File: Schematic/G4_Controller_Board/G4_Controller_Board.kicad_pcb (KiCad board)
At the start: 2 copper layers, 30 parts, among them J10 12 Volts In, J11 Preset A, J12 Voltmeter, J13 Preset B, J14 Preset C, J15 Combined Preset Connector, J16 Rev Trigger (Optional), J17 Fire Trigger, J18 Magazine Removal Trigger, J19 Rotary Encoder, J2 Screw_Terminal_01x02, J20 I2C Out, J21 ESC Right, J22 ESC Left, J25 IR LED Rec., J26 IR LED Emitter, J6 Solenoid, Q1 IRF540N, U1 Mini360, U2 ESP32-LOLIN32-Lite

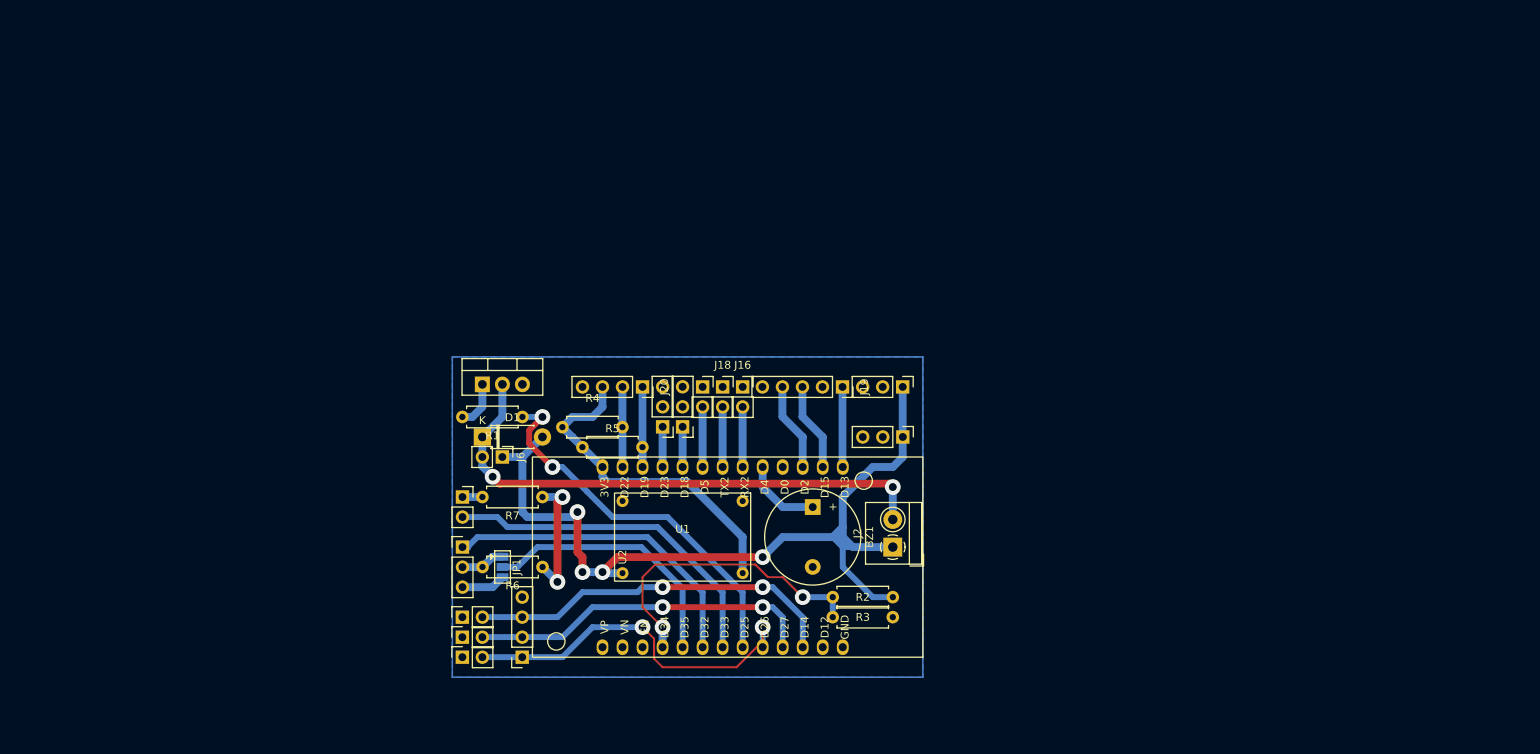
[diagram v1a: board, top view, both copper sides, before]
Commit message: begin work on new PCB
2 layers with fast decay driver
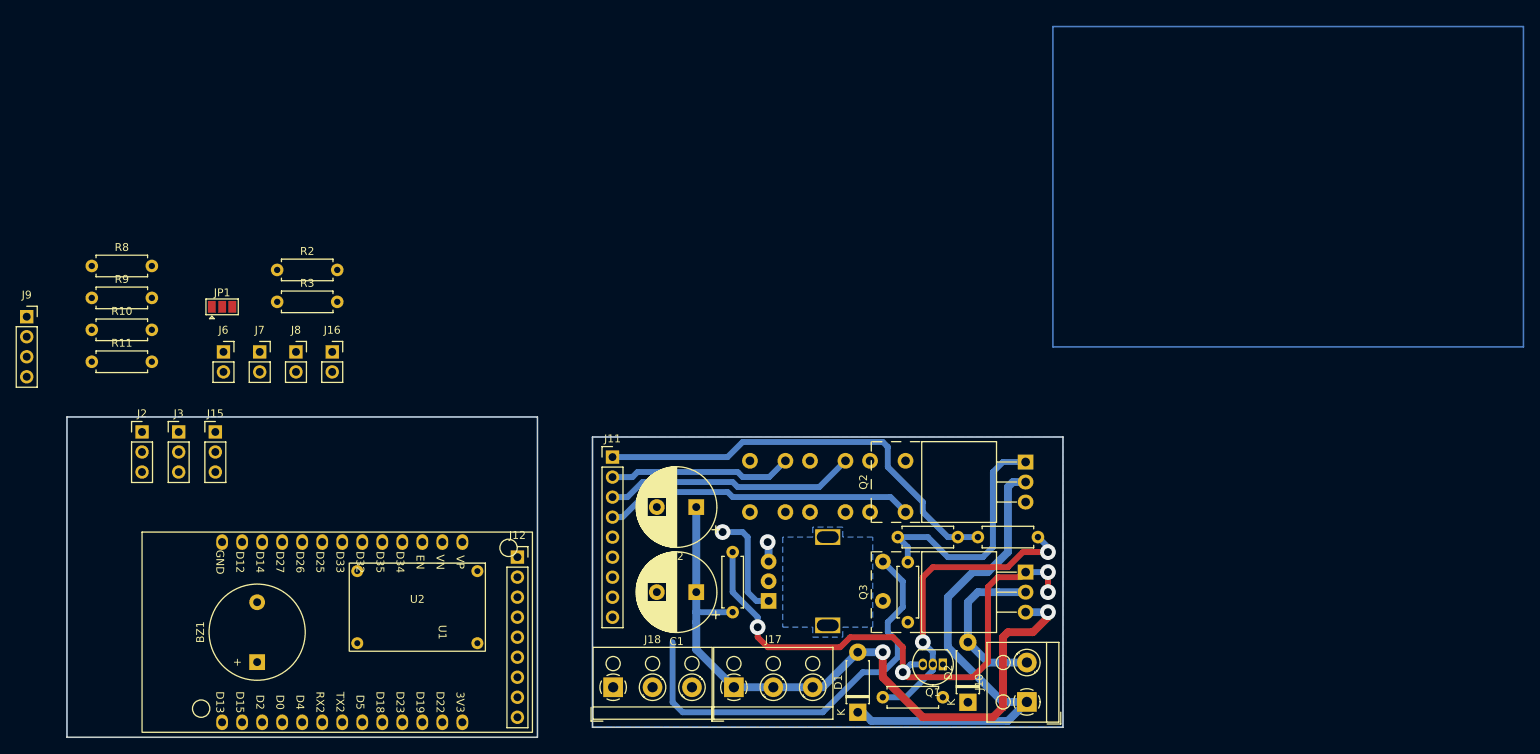
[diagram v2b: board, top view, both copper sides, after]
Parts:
- removed J13: Preset B, Connector_PinSocket_2.54mm:PinSocket_1x02_P2.54mm_Vertical
- removed J14: Preset C, Connector_PinSocket_2.54mm:PinSocket_1x02_P2.54mm_Vertical
- removed J19: Rotary Encoder, Connector_PinSocket_2.54mm:PinSocket_1x05_P2.54mm_Vertical
- removed J20: I2C Out, Connector_PinSocket_2.54mm:PinSocket_1x04_P2.54mm_Vertical
- removed J21: ESC Right, Connector_PinHeader_2.54mm:PinHeader_1x03_P2.54mm_Vertical
- removed J22: ESC Left, Connector_PinHeader_2.54mm:PinHeader_1x03_P2.54mm_Vertical
- removed J25: IR LED Rec., Connector_PinHeader_2.54mm:PinHeader_1x03_P2.54mm_Vertical
- removed J26: IR LED Emitter, Connector_PinSocket_2.54mm:PinSocket_1x02_P2.54mm_Vertical
- added C1: 470uF, Capacitor_THT:CP_Radial_D10.0mm_P5.00mm, F.Cu at (133.8, 92.1)
- added C2: 470uF, Capacitor_THT:CP_Radial_D10.0mm_P5.00mm, F.Cu at (133.8, 81.3)
- added D2: DIODE, Diode_THT:D_DO-41_SOD81_P7.62mm_Horizontal, F.Cu at (168.3, 106.0)
- added J3: ESC Left, Connector_PinHeader_2.54mm:PinHeader_1x03_P2.54mm_Vertical, F.Cu at (68.2, 71.8)
- added J7: Fire Trigger, Connector_PinSocket_2.54mm:PinSocket_1x02_P2.54mm_Vertical, F.Cu at (78.4, 61.6)
- added J8: Magazine Removal Trigger, Connector_PinSocket_2.54mm:PinSocket_1x02_P2.54mm_Vertical, F.Cu at (83.0, 61.6)
- added J9: I2C Out, Connector_PinSocket_2.54mm:PinSocket_1x04_P2.54mm_Vertical, F.Cu at (48.9, 57.1)
- added Q2: Q_NMOS_GDS, Package_TO_SOT_THT:TO-220-3_Horizontal_TabUp, F.Cu at (175.6, 75.6)
- added Q3: Q_PMOS_GDS, Package_TO_SOT_THT:TO-220-3_Horizontal_TabUp, F.Cu at (175.6, 89.5)
- added R10: 10K Ohm, Resistor_THT:R_Axial_DIN0207_L6.3mm_D2.5mm_P7.62mm_Horizontal, F.Cu at (57.1, 58.8)
- added R11: 90 Ohm, Resistor_THT:R_Axial_DIN0207_L6.3mm_D2.5mm_P7.62mm_Horizontal, F.Cu at (57.1, 62.8)
- added R8: 2.4k Ohm, Resistor_THT:R_Axial_DIN0207_L6.3mm_D2.5mm_P7.62mm_Horizontal, F.Cu at (57.1, 50.7)
- added R9: 2.4k Ohm, Resistor_THT:R_Axial_DIN0207_L6.3mm_D2.5mm_P7.62mm_Horizontal, F.Cu at (57.1, 54.7)
- added SW2: Preset A, Button_Switch_THT:SW_PUSH_6mm_H13mm, B.Cu at (155.9, 75.4)
- added SW3: Preset B, Button_Switch_THT:SW_PUSH_6mm_H13mm, B.Cu at (148.2, 75.4)
- added SW4: Preset C, Button_Switch_THT:SW_PUSH_6mm_H13mm, B.Cu at (140.6, 75.4)
- added SW7: RotaryEncoder_Switch, Rotary_Encoder:RotaryEncoder_Alps_EC11E-Switch_Vertical_H20mm, B.Cu at (143.0, 93.2)
- D1: value IN4001 -> DIODE
- J10: value 12 Volts In -> Solenoid; footprint Connector_PinHeader_2.54mm:PinHeader_1x03_P2.54mm_Vertical -> TerminalBlock_RND:TerminalBlock_RND_205-00001_1x02_P5.00mm_Horizontal
- J11: value Preset A -> Inter-board Jumper; footprint Connector_PinSocket_2.54mm:PinSocket_1x02_P2.54mm_Vertical -> Connector_PinHeader_2.54mm:PinHeader_1x09_P2.54mm_Vertical
- J12: value Voltmeter -> Inter-board Jumper; footprint Connector_PinHeader_2.54mm:PinHeader_1x03_P2.54mm_Vertical -> Connector_PinSocket_2.54mm:PinSocket_1x09_P2.54mm_Vertical
- J15: value Combined Preset Connector -> IR LED Rec.; footprint Connector_PinSocket_2.54mm:PinSocket_1x04_P2.54mm_Vertical -> Connector_PinHeader_2.54mm:PinHeader_1x03_P2.54mm_Vertical
- J16: value Rev Trigger (Optional) -> IR LED Emitter
- J17: value Fire Trigger -> Positive BUS; footprint Connector_PinSocket_2.54mm:PinSocket_1x02_P2.54mm_Vertical -> TerminalBlock_RND:TerminalBlock_RND_205-00002_1x03_P5.00mm_Horizontal
- J18: value Magazine Removal Trigger -> Negative BUS; footprint Connector_PinSocket_2.54mm:PinSocket_1x02_P2.54mm_Vertical -> TerminalBlock_RND:TerminalBlock_RND_205-00002_1x03_P5.00mm_Horizontal
- J2: value Screw_Terminal_01x02 -> ESC Right; footprint TerminalBlock_4Ucon:TerminalBlock_4Ucon_1x02_P3.50mm_Horizontal -> Connector_PinHeader_2.54mm:PinHeader_1x03_P2.54mm_Vertical
- J6: value Solenoid -> Rev Trigger (Optional); footprint Connector_PinHeader_2.54mm:PinHeader_1x02_P2.54mm_Vertical -> Connector_PinSocket_2.54mm:PinSocket_1x02_P2.54mm_Vertical
- Q1: value IRF540N -> 2N7000; footprint Package_TO_SOT_THT:TO-220-3_Vertical -> Package_TO_SOT_THT:TO-92_Inline
- R1: value 220 -> 10KR
- R4: value 2.4k Ohm -> 10KR
- R5: value 2.4k Ohm -> 100R
- R6: value 10K Ohm -> 10KR
- R7: value 90 Ohm -> 100R
- U1: value Mini360 -> ESP32-LOLIN32-Lite; footprint My_Library:Mini360 -> Espressif:ESP32-LOLIN32-Lite
- U2: value ESP32-LOLIN32-Lite -> Mini360; footprint Espressif:ESP32-LOLIN32-Lite -> My_Library:Mini360
- moved J2 96.4 mm to (63.5, 71.8), turned to 0 degrees
- moved R3 87.8 mm to (80.6, 55.2), turned to 0 degrees
- moved R2 81.8 mm to (80.6, 51.2)
- moved BZ1 73.2 mm to (78.1, 101.0), turned to 90 degrees
- moved Q1 68.4 mm to (165.1, 101.2), turned to 180 degrees
- moved R4 59.2 mm to (165.1, 105.4), turned to 180 degrees
- moved D1 59.1 mm to (154.3, 107.3), turned to 90 degrees
- moved R5 58.9 mm to (177.2, 85.1), turned to 180 degrees
- moved J16 52.3 mm to (87.6, 61.6)
- moved J12 51.2 mm to (111.1, 87.6), turned to 0 degrees
- moved JP1 48.5 mm to (73.7, 55.9), turned to 0 degrees
- moved J15 48.3 mm to (72.8, 71.8), turned to 0 degrees
- moved R6 46.9 mm to (160.7, 95.9), turned to 90 degrees
- moved R7 45.4 mm to (159.4, 85.1), turned to 0 degrees
- moved U1 44.8 mm to (88.9, 97.2), turned to -90 degrees
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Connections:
- D1 pad 1: Net-(D1-Pad1) -> /SOLENOID_A
- J10 pad 1: +12V -> /SOLENOID_A
- J10 pad 2: GND -> /SOLENOID_B
- J11 pad 1: GND -> /Pusher Pin
- J11 pad 2: /Preset A -> /Preset C
- J12 pad 1: +12V -> /Pusher Pin
- J12 pad 2: GND -> /Preset C
- J12 pad 3: unconnected-(J12-Pad3) -> /Preset B
- J15 pad 1: /Preset C -> /IR Rec. Supply
- J15 pad 2: /Preset B -> Net-(J15-Pin_2)
- J15 pad 3: /Preset A -> Net-(J15-Pin_3)
- J16 pad 1: GND -> Net-(J16-Pin_1)
- J16 pad 2: /RevTrg -> /IR Emitter
- J17 pad 1: GND -> +12V
- J17 pad 2: /FireTrg -> +12V
- J18 pad 2: /MagTrg -> GND
- J2 pad 1: +12V -> /ESC Right
- J2 pad 2: Net-(D1-Pad1) -> unconnected-(J2-Pin_2-Pad2)
- J6 pad 1: +12V -> GND
- J6 pad 2: Net-(D1-Pad1) -> /RevTrg
- JP1 pad 1: Net-(J25-Pad2) -> Net-(J15-Pin_2)
- JP1 pad 3: Net-(J25-Pad3) -> Net-(J15-Pin_3)
- Q1 pad 1: Net-(Q1-Pad1) -> GND
- Q1 pad 2: Net-(D1-Pad1) -> /High Side Driver
- Q1 pad 3: GND -> Net-(Q1-D)
- R1 pad 1: /PUSHER PIN -> +12V
- R1 pad 2: Net-(Q1-Pad1) -> Net-(Q1-D)
- R4 pad 1: +3V3 -> GND
- R4 pad 2: /SCL/SCK (Clock) -> /High Side Driver
- R5 pad 1: +3V3 -> /High Side Driver
- R5 pad 2: /SDA/SDI (Data) -> /Pusher Pin
- R6 pad 2: Net-(J25-Pad2) -> /Low Side Driver
- R7 pad 1: GND -> /Low Side Driver
- R7 pad 2: Net-(J26-Pad1) -> /Pusher Pin
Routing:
- net Net-(Q1-D): track 0.00 -> 70.6 mm, vias 0 -> 4
- net Net-(D1-Pad1): track 68.7 -> 0.00 mm, vias 2 -> 0
- net /SOLENOID_A: track 0.00 -> 62.9 mm
- net /Pusher Pin: track 0.00 -> 54.4 mm
- net /PUSHER PIN: track 48.8 -> 0.00 mm, vias 2 -> 0
- net /Encoder Switch: track 10.2 -> 54.1 mm
- net /IR Emitter: track 43.9 -> 0.00 mm
- net +3V3: track 42.7 -> 0.00 mm
- net /IR Rec. Supply: track 40.9 -> 0.00 mm
- net /High Side Driver: track 0.00 -> 39.7 mm, vias 0 -> 2
- net /Battery Reader: track 39.0 -> 0.00 mm, vias 2 -> 0
- net /IR Reciever: track 33.5 -> 0.00 mm
- net /Low Side Driver: track 0.00 -> 31.5 mm
- net /Preset C: track 46.5 -> 23.3 mm, vias 2 -> 0
- net +12V: track 113.1 -> 90.4 mm, vias 4 -> 2
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- added copper zone on B.Cu, net Tab
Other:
- board outline added: 126.4 x 40.6 mm
- board text added: "Side 1"
- board text added: "Side 2"

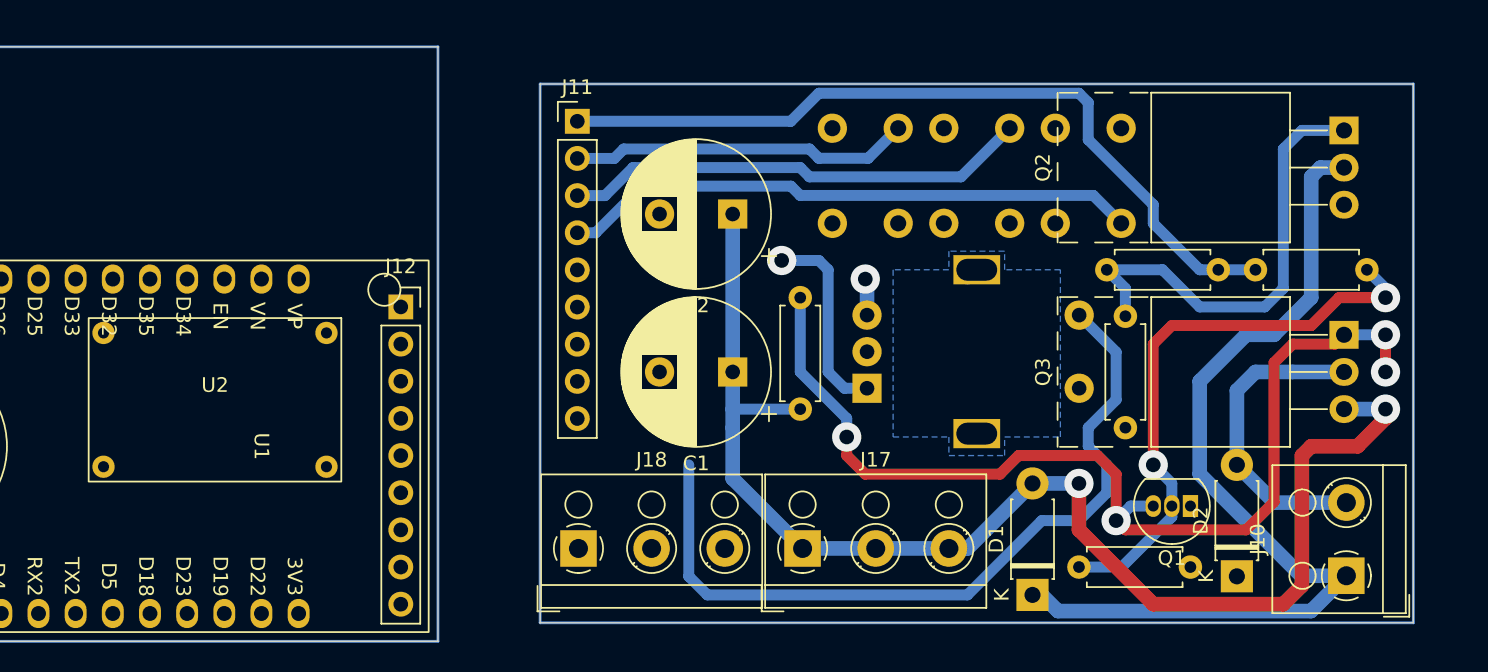
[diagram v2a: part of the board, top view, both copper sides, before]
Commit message: update the PCB
added more traces
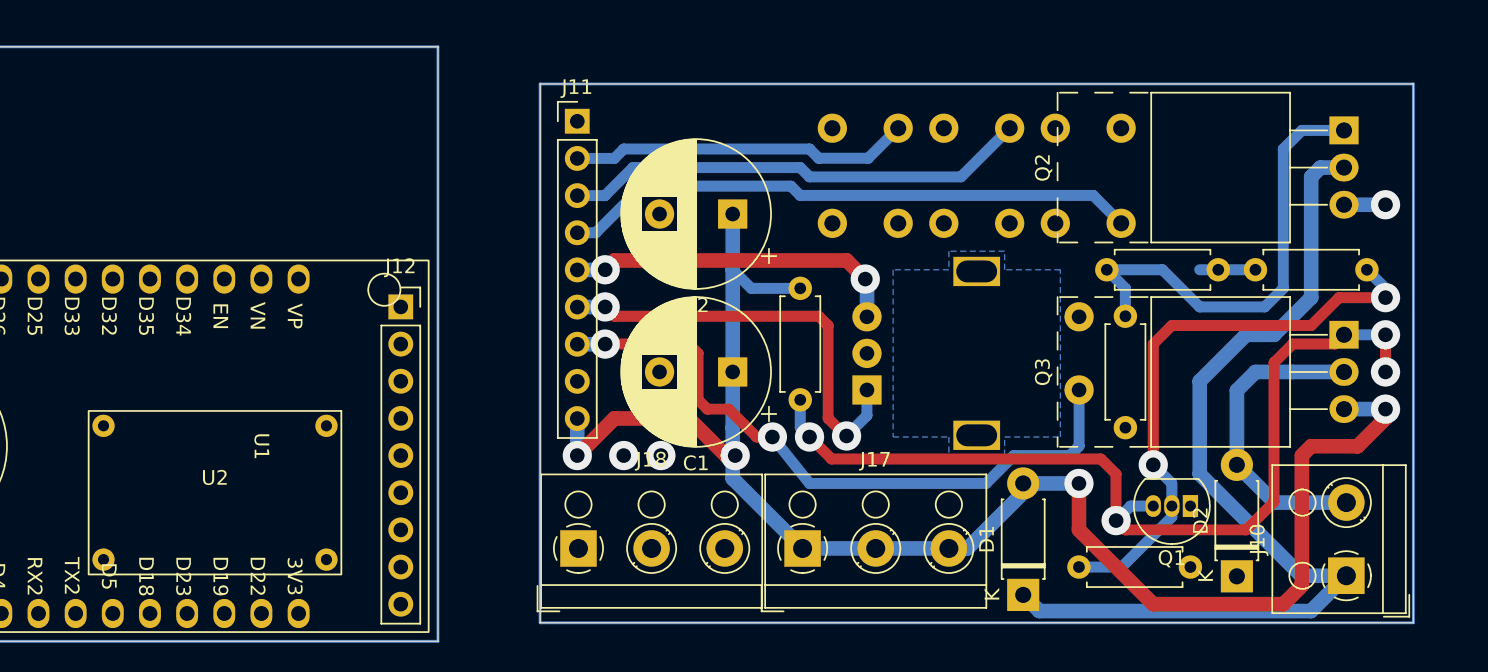
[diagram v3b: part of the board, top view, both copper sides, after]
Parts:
- moved R1 8.25 mm to (138.4, 86.4), turned to -90 degrees
- moved U2 6.35 mm to (98.4, 100.3)
- moved D1 0.64 mm to (153.7, 107.3)
- moved SW7 0.12 mm to (143.0, 93.3)
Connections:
- J11 pad 5: /Encoder A -> /Encoder B
- J11 pad 6: /Encoder B -> /Encoder A
- J12 pad 5: /Encoder A -> /Encoder B
- J12 pad 6: /Encoder B -> /Encoder A
- SW7 pad S1: /Encoder Switch -> GND
- SW7 pad S2: GND -> /Encoder Switch
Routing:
- net /Pusher Pin: track 54.4 -> 3.81 mm
- net /Encoder B: track 2.51 -> 23.0 mm, vias 1 -> 2
- net +12V: track 90.4 -> 106.5 mm, vias 2 -> 4
- net /Encoder A: track 13.5 -> 29.5 mm, vias 1 -> 2
- net /Encoder Switch: track 54.1 -> 45.9 mm, vias 0 -> 2
- net Net-(Q1-D): track 70.6 -> 63.3 mm
- net GND: track 0.00 -> 2.84 mm, vias 0 -> 3
- net /SOLENOID_A: track 62.9 -> 63.6 mm
